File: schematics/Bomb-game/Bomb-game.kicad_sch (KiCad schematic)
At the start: 10 parts, among them J1 Joystick, U1 ADKeyboard, U2 Relays x4, U3 Emergency Button, U4 Buzzer, U5 Buzzer, U6 8x8 WS2812B, U7 LCD 1602, U8 3x4 keypad

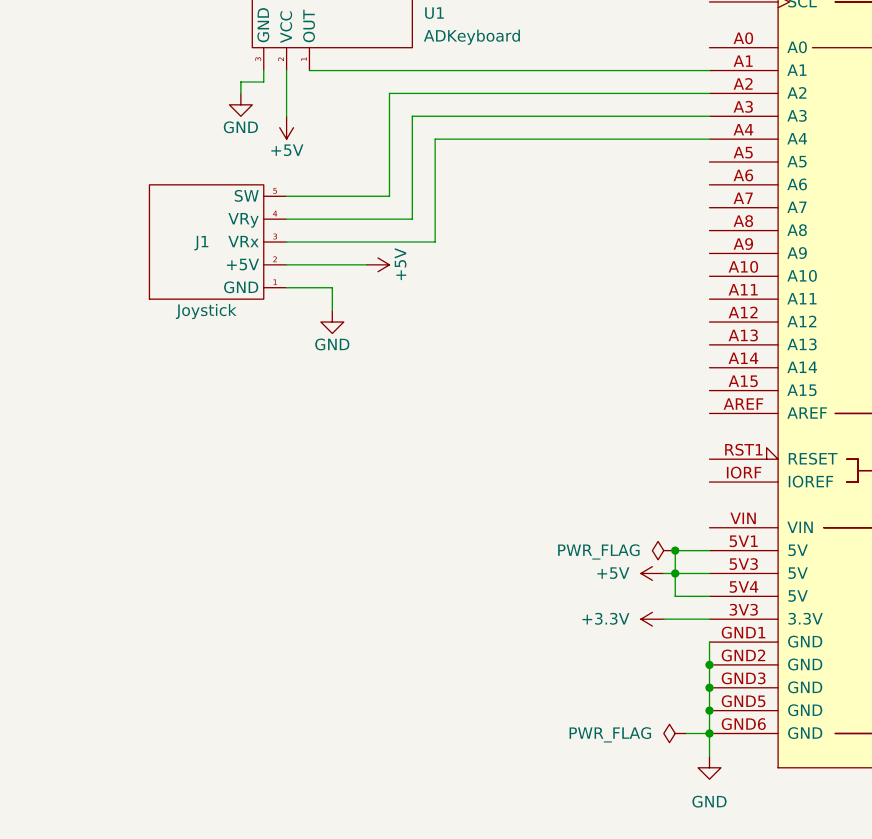
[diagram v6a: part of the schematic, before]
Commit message: Add potenciometer tests
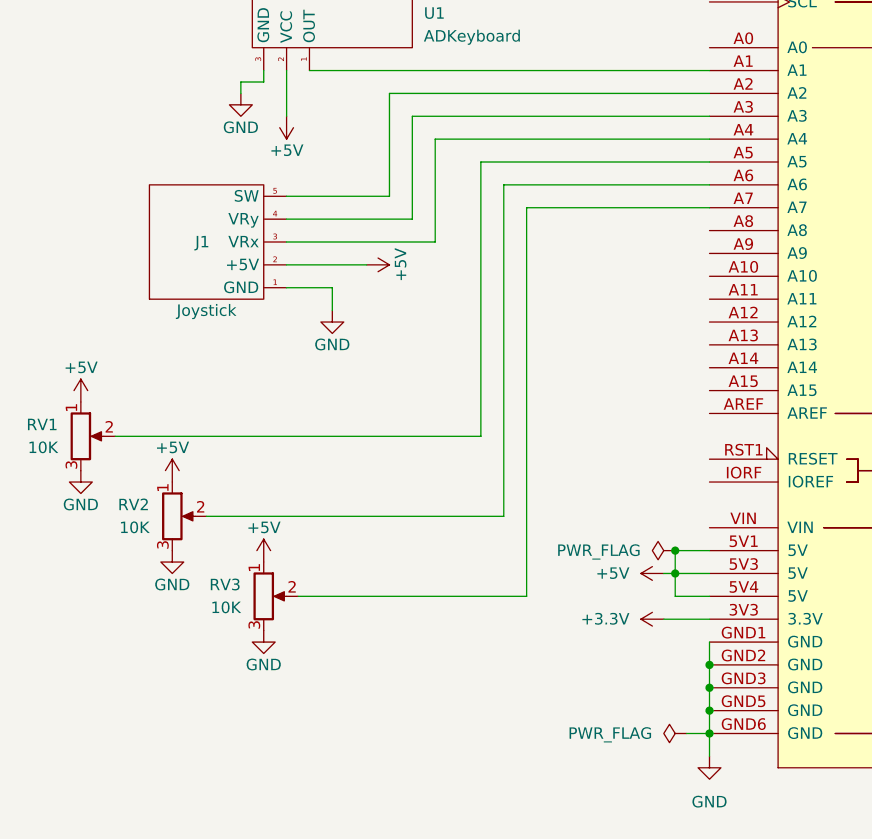
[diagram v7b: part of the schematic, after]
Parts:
- added RV1, RV2, RV3: 10K, symbol Device:R_Potentiometer
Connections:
- net +5V: now also RV1.1, RV2.1, RV3.1
- net GND: now also RV1.3, RV2.3, RV3.3
- net at XA1.A5: now also RV1.2
- net at XA1.A6: now also RV2.2
- net at XA1.A7: now also RV3.2
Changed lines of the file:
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@@
+    (stroke (width 0) (type default))
+  )
+  (wire (pts (xy 63.5 133.35) (xy 88.9 133.35))
     (stroke (width 0) (type default))
   )
@@
     (stroke (width 0) (type default))
   )
+  (wire (pts (xy 83.82 115.57) (xy 83.82 85.09))
+    (stroke (width 0) (type default))
+  )
   (wire (pts (xy 175.26 69.85) (xy 226.06 69.85))
     (stroke (width 0) (type default))
@@
     (stroke (width 0) (type default))
   )
+  (wire (pts (xy 83.82 85.09) (xy 109.22 85.09))
+    (stroke (width 0) (type default))
+  )
   (wire (pts (xy 203.2 58.42) (xy 205.74 58.42))
     (stroke (width 0) (type default))
@@
     (stroke (width 0) (type default))
   )
+  (wire (pts (xy 88.9 133.35) (xy 88.9 90.17))
+    (stroke (width 0) (type default))
+  )
   (wire (pts (xy 226.06 69.85) (xy 226.06 62.23))
     (stroke (width 0) (type default))
@@
     (stroke (width 0) (type default))
   )
+  (wire (pts (xy 88.9 90.17) (xy 109.22 90.17))
+    (stroke (width 0) (type default))
+  )
   (wire (pts (xy 201.93 110.49) (xy 175.26 110.49))
     (stroke (width 0) (type default))
@@
     (stroke (width 0) (type default))
   )
+  (wire (pts (xy 86.36 87.63) (xy 109.22 87.63))
+    (stroke (width 0) (type default))
+  )
   (wire (pts (xy 232.41 130.81) (xy 232.41 142.24))
     (stroke (width 0) (type default))
@@
     (stroke (width 0) (type default))
   )
+  (wire (pts (xy 86.36 124.46) (xy 86.36 87.63))
+    (stroke (width 0) (type default))
+  )
+  (wire (pts (xy 43.18 115.57) (xy 83.82 115.57))
+    (stroke (width 0) (type default))
+  )
   (wire (pts (xy 76.2 80.01) (xy 109.22 80.01))
     (stroke (width 0) (type default))
@@
     (stroke (width 0) (type default))
   )
+  (wire (pts (xy 53.34 124.46) (xy 86.36 124.46))
+    (stroke (width 0) (type default))
+  )
   (wire (pts (xy 175.26 62.23) (xy 205.74 62.23))
     (stroke (width 0) (type default))
@@
     (stroke (width 0) (type default))
   )
+  (symbol (lib_id "Device:R_Potentiometer") (at 39.37 115.57 0) (unit 1)
+    (in_bom yes) (on_board yes) (dnp no) (fields_autoplaced)
+    (property "Reference" "RV1" (at 36.83 114.3 0)
+      (effects (font (size 1.27 1.27)) (justify right))
+    )
+    (property "Value" "10K" (at 36.83 116.84 0)
+      (effects (font (size 1.27 1.27)) (justify right))
+    )
+    (property "Footprint" "" (at 39.37 115.57 0)
+      (effects (font (size 1.27 1.27)) hide)
+    )
+    (property "Datasheet" "~" (at 39.37 115.57 0)
+      (effects (font (size 1.27 1.27)) hide)
+    )
+    (pin "1")
+    (pin "2")
+    (pin "3")
+    (instances
+      (project "Bomb-game"
+        (path "/d5dfcc17-2f57-46e4-9b81-9957aca5a4a9"
+          (reference "RV1") (unit 1)
+        )
+      )
+    )
+  )
   (symbol (lib_id "power:GND") (at 67.31 101.6 0) (unit 1)
     (in_bom yes) (on_board yes) (dnp no)
@@
         (path "/d5dfcc17-2f57-46e4-9b81-9957aca5a4a9"
           (reference "#PWR07") (unit 1)
+        )
+      )
+    )
+  )
+  (symbol (lib_id "power:GND") (at 49.53 128.27 0) (unit 1)
+    (in_bom yes) (on_board yes) (dnp no)
+    (property "Reference" "#PWR020" (at 49.53 134.62 0)
+      (effects (font (size 1.27 1.27)) hide)
+    )
+    (property "Value" "GND" (at 49.53 132.08 0)
+      (effects (font (size 1.27 1.27)))
+    )
+    (property "Footprint" "" (at 49.53 128.27 0)
+      (effects (font (size 1.27 1.27)) hide)
+    )
+    (property "Datasheet" "" (at 49.53 128.27 0)
+      (effects (font (size 1.27 1.27)) hide)
+    )
+    (pin "1")
+    (instances
+      (project "Bomb-game"
+        (path "/d5dfcc17-2f57-46e4-9b81-9957aca5a4a9"
+          (reference "#PWR020") (unit 1)
         )
       )
@@
         (path "/d5dfcc17-2f57-46e4-9b81-9957aca5a4a9"
           (reference "#PWR03") (unit 1)
+        )
+      )
+    )
+  )
+  (symbol (lib_id "Device:R_Potentiometer") (at 59.69 133.35 0) (unit 1)
+    (in_bom yes) (on_board yes) (dnp no) (fields_autoplaced)
+    (property "Reference" "RV3" (at 57.15 132.08 0)
+      (effects (font (size 1.27 1.27)) (justify right))
+    )
+    (property "Value" "10K" (at 57.15 134.62 0)
+      (effects (font (size 1.27 1.27)) (justify right))
+    )
+    (property "Footprint" "" (at 59.69 133.35 0)
+      (effects (font (size 1.27 1.27)) hide)
+    )
+    (property "Datasheet" "~" (at 59.69 133.35 0)
+      (effects (font (size 1.27 1.27)) hide)
+    )
+    (pin "1")
+    (pin "2")
+    (pin "3")
+    (instances
+      (project "Bomb-game"
+        (path "/d5dfcc17-2f57-46e4-9b81-9957aca5a4a9"
+          (reference "RV3") (unit 1)
+        )
+      )
+    )
+  )
+  (symbol (lib_id "power:GND") (at 59.69 137.16 0) (unit 1)
+    (in_bom yes) (on_board yes) (dnp no)
+    (property "Reference" "#PWR022" (at 59.69 143.51 0)
+      (effects (font (size 1.27 1.27)) hide)
+    )
+    (property "Value" "GND" (at 59.69 140.97 0)
+      (effects (font (size 1.27 1.27)))
+    )
+    (property "Footprint" "" (at 59.69 137.16 0)
+      (effects (font (size 1.27 1.27)) hide)
+    )
+    (property "Datasheet" "" (at 59.69 137.16 0)
+      (effects (font (size 1.27 1.27)) hide)
+    )
+    (pin "1")
+    (instances
+      (project "Bomb-game"
+        (path "/d5dfcc17-2f57-46e4-9b81-9957aca5a4a9"
+          (reference "#PWR022") (unit 1)
         )
       )
@@
     )
   )
+  (symbol (lib_id "Device:R_Potentiometer") (at 49.53 124.46 0) (unit 1)
+    (in_bom yes) (on_board yes) (dnp no) (fields_autoplaced)
+    (property "Reference" "RV2" (at 46.99 123.19 0)
+      (effects (font (size 1.27 1.27)) (justify right))
+    )
+    (property "Value" "10K" (at 46.99 125.73 0)
+      (effects (font (size 1.27 1.27)) (justify right))
+    )
+    (property "Footprint" "" (at 49.53 124.46 0)
+      (effects (font (size 1.27 1.27)) hide)
+    )
+    (property "Datasheet" "~" (at 49.53 124.46 0)
+      (effects (font (size 1.27 1.27)) hide)
+    )
+    (pin "1")
+    (pin "2")
+    (pin "3")
+    (instances
+      (project "Bomb-game"
+        (path "/d5dfcc17-2f57-46e4-9b81-9957aca5a4a9"
+          (reference "RV2") (unit 1)
+        )
+      )
+    )
+  )
   (symbol (lib_id "Bomb-parts:ADKeyboard") (at 66.04 69.85 0) (unit 1)
     (in_bom yes) (on_board yes) (dnp no) (fields_autoplaced)
@@
         (path "/d5dfcc17-2f57-46e4-9b81-9957aca5a4a9"
           (reference "#PWR01") (unit 1)
+        )
+      )
+    )
+  )
+  (symbol (lib_id "power:GND") (at 39.37 119.38 0) (unit 1)
+    (in_bom yes) (on_board yes) (dnp no)
+    (property "Reference" "#PWR018" (at 39.37 125.73 0)
+      (effects (font (size 1.27 1.27)) hide)
+    )
+    (property "Value" "GND" (at 39.37 123.19 0)
+      (effects (font (size 1.27 1.27)))
+    )
+    (property "Footprint" "" (at 39.37 119.38 0)
+      (effects (font (size 1.27 1.27)) hide)
+    )
+    (property "Datasheet" "" (at 39.37 119.38 0)
+      (effects (font (size 1.27 1.27)) hide)
+    )
+    (pin "1")
+    (instances
+      (project "Bomb-game"
+        (path "/d5dfcc17-2f57-46e4-9b81-9957aca5a4a9"
+          (reference "#PWR018") (unit 1)
         )
       )
@@
     )
   )
+  (symbol (lib_id "power:+5V") (at 49.53 120.65 0) (unit 1)
+    (in_bom yes) (on_board yes) (dnp no)
+    (property "Reference" "#PWR019" (at 49.53 124.46 0)
+      (effects (font (size 1.27 1.27)) hide)
+    )
+    (property "Value" "+5V" (at 49.53 116.84 0)
+      (effects (font (size 1.27 1.27)))
+    )
+    (property "Footprint" "" (at 49.53 120.65 0)
+      (effects (font (size 1.27 1.27)) hide)
+    )
+    (property "Datasheet" "" (at 49.53 120.65 0)
+      (effects (font (size 1.27 1.27)) hide)
+    )
+    (pin "1")
+    (instances
+      (project "Bomb-game"
+        (path "/d5dfcc17-2f57-46e4-9b81-9957aca5a4a9"
+          (reference "#PWR019") (unit 1)
+        )
+      )
+    )
+  )
   (symbol (lib_id "Bomb-parts:Relay_x4") (at 262.89 86.36 270) (unit 1)
     (in_bom yes) (on_board yes) (dnp no)
@@
         (path "/d5dfcc17-2f57-46e4-9b81-9957aca5a4a9"
           (reference "#PWR06") (unit 1)
+        )
+      )
+    )
+  )
+  (symbol (lib_id "power:+5V") (at 59.69 129.54 0) (unit 1)
+    (in_bom yes) (on_board yes) (dnp no)
+    (property "Reference" "#PWR021" (at 59.69 133.35 0)
+      (effects (font (size 1.27 1.27)) hide)
+    )
+    (property "Value" "+5V" (at 59.69 125.73 0)
+      (effects (font (size 1.27 1.27)))
+    )
+    (property "Footprint" "" (at 59.69 129.54 0)
+      (effects (font (size 1.27 1.27)) hide)
+    )
+    (property "Datasheet" "" (at 59.69 129.54 0)
+      (effects (font (size 1.27 1.27)) hide)
+    )
+    (pin "1")
+    (instances
+      (project "Bomb-game"
+        (path "/d5dfcc17-2f57-46e4-9b81-9957aca5a4a9"
+          (reference "#PWR021") (unit 1)
         )
       )
@@
         )
       )
+    )
+  )
+  (symbol (lib_id "power:+5V") (at 39.37 111.76 0) (unit 1)
+    (in_bom yes) (on_board yes) (dnp no)
+    (property "Reference" "#PWR017" (at 39.37 115.57 0)
+      (effects (font (size 1.27 1.27)) hide)
+    )
+    (property "Value" "+5V" (at 39.37 107.95 0)
+      (effects (font (size 1.27 1.27)))
+    )
+    (property "Footprint" "" (at 39.37 111.76 0)
+      (effects (font (size 1.27 1.27)) hide)
+    )
+    (property "Datasheet" "" (at 39.37 111.76 0)
+      (effects (font (size 1.27 1.27)) hide)
+    )
+    (pin "1")
+    (instances
+      (project "Bomb-game"
+        (path "/d5dfcc17-2f57-46e4-9b81-9957aca5a4a9"
+          (reference "#PWR017") (unit 1)
+        )
+      )

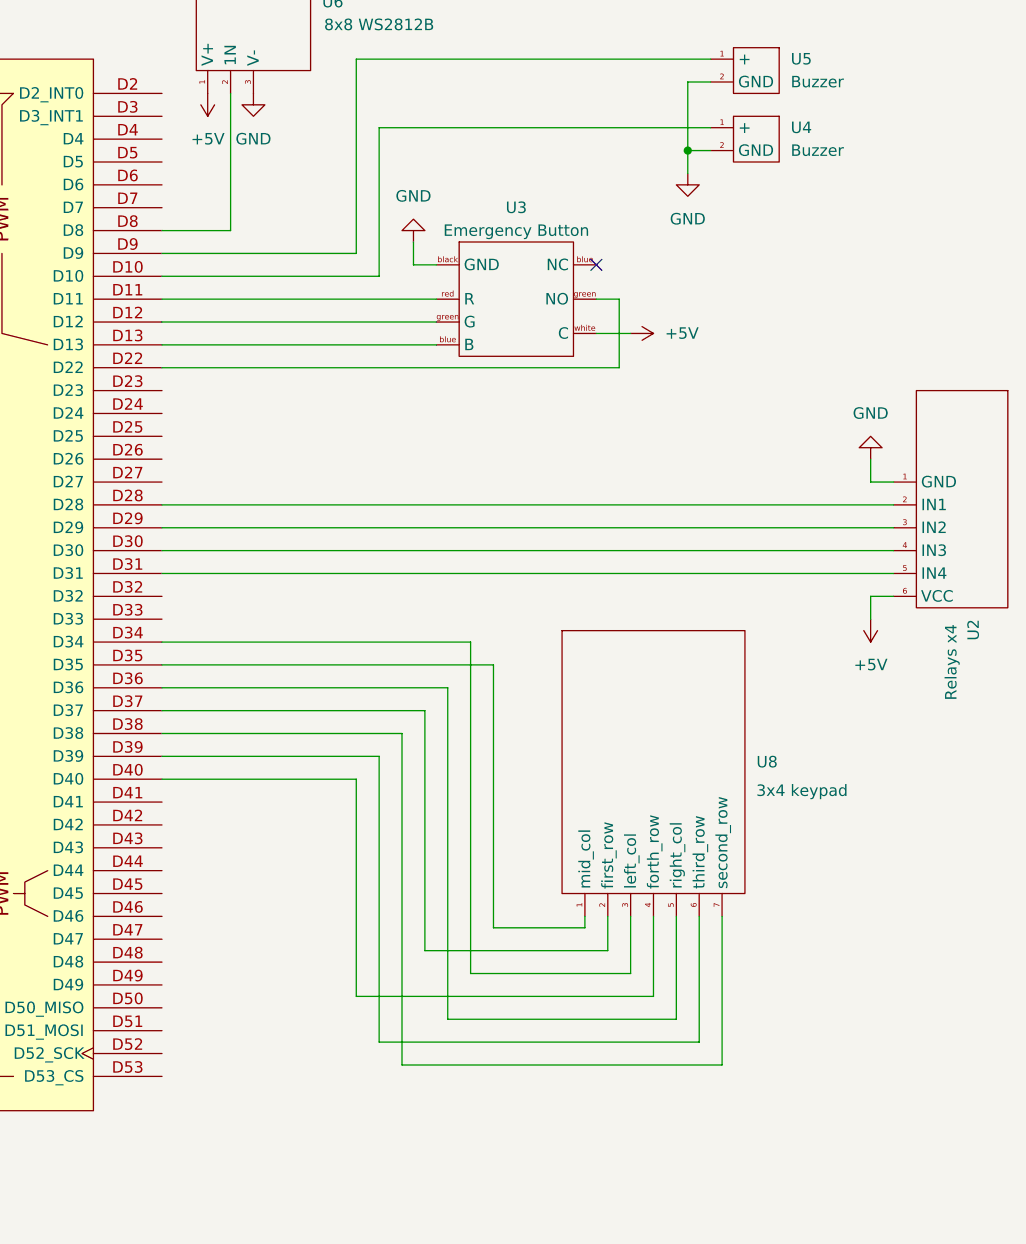
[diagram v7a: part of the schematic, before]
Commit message: Finish all components connections
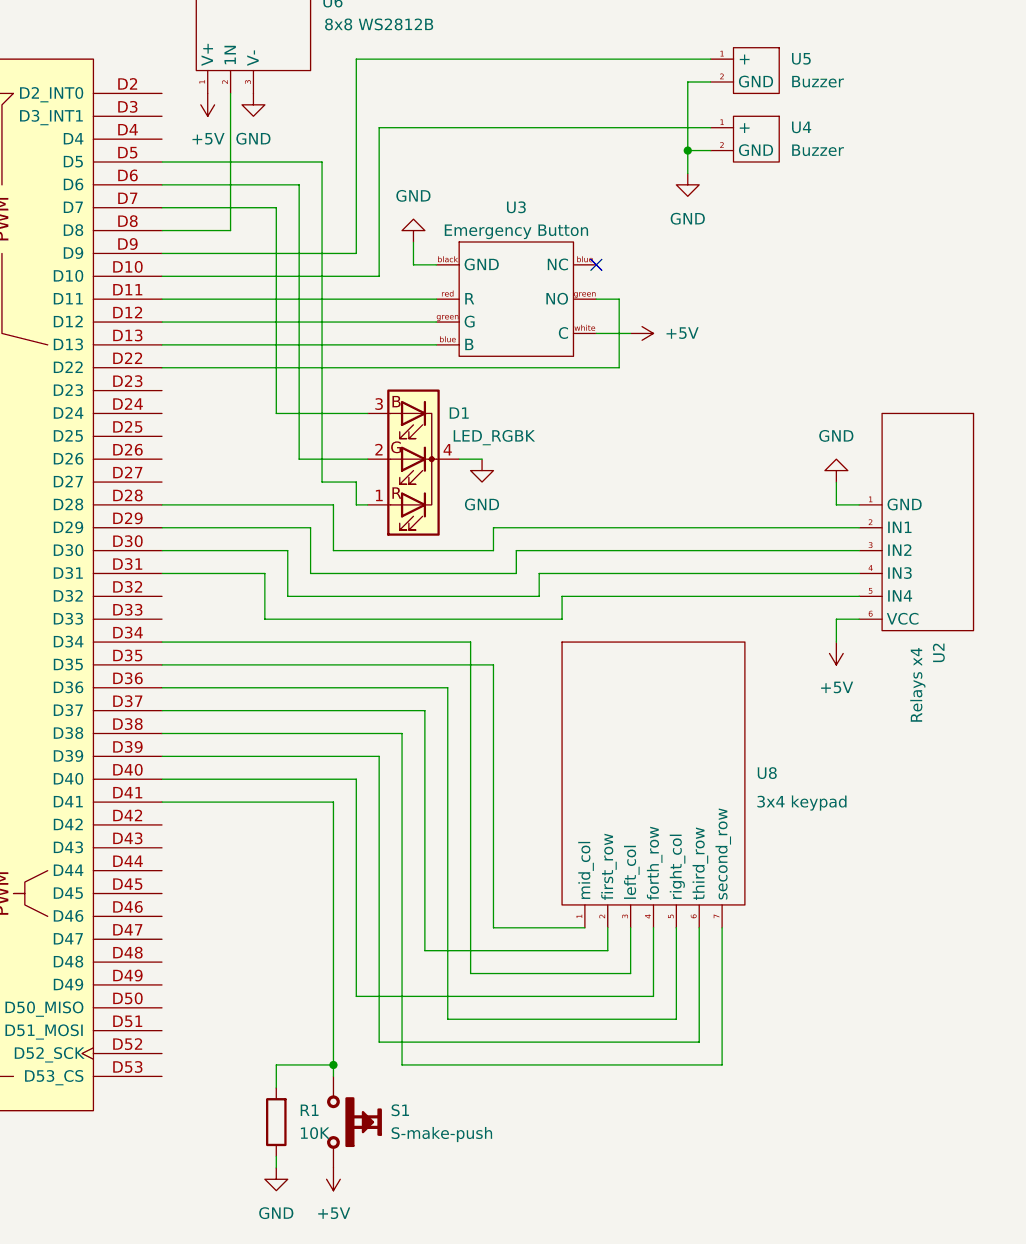
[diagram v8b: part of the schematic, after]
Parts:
- added D1: LED_RGBK, symbol Device:LED_RGBK
- added R1: 10K, symbol Device:R
- added S1: S-make-push, symbol PCM_Elektuur:S-make-push
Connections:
- net +5V: now also S1.4
- net GND: now also D1.4 (K), R1.1
- net at XA1.D41: now also R1.2, S1.3
- net at XA1.D5: now also D1.1 (RA)
- net at XA1.D6: now also D1.2 (GA)
- net at XA1.D7: now also D1.3 (BA)
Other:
- moved on the sheet: U2, U8
